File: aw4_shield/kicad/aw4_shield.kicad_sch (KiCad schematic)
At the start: 73 parts, among them J1 J1 +12V / PGND, J2 JP1 5V -> Nano (jumper), J3 J6 rezerva, J4 J2 SOL1-3 / TCU1-3, J5 J3 UP DOWN READY LOCKUP, J6 J5 Nextion +5V GND RX TX, K1 G5LE-1 12V SPDT, K2 G5LE-1 12V SPDT, K3 G5LE-1 12V SPDT, Q1 IRF4905, Q2 BC337, Q3 IRF9540N, Q4 IRF9540N, Q5 IRF9540N, U1 Buck 12V->5V 1A (modul), U2 Arduino Nano, U3 PC817, U4 PC817, U5 PC817, U6 PC817

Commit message: AW4 shield: connector references match docs
Co-Authored-By: Claude Sonnet 5.5 <noreply@anthropic.com>
Claude-Session: https://claude.ai/code/session_01QHDQqfFe1juWLgZ1EWa6E5
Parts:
- removed J2: JP1 5V -> Nano (jumper), Connector_PinHeader_2.54mm:PinHeader_1x02_P2.54mm_Vertical, symbol AW4:CONN2
- removed J3: J6 rezerva, Connector_PinHeader_2.54mm:PinHeader_1x07_P2.54mm_Vertical, symbol AW4:CONN7
- removed J4: J2 SOL1-3 / TCU1-3, TerminalBlock_Phoenix:TerminalBlock_Phoenix_MKDS-1,5-6-5.08_1x06_P5.08mm_Horizontal, symbol AW4:CONN6
- removed J5: J3 UP DOWN READY LOCKUP, TerminalBlock_Phoenix:TerminalBlock_Phoenix_MKDS-1,5-6-5.08_1x06_P5.08mm_Horizontal, symbol AW4:CONN6
- removed J6: J5 Nextion +5V GND RX TX, Connector_JST:JST_XH_B4B-XH-A_1x04_P2.50mm_Vertical, symbol AW4:CONN4
- added J2: J2 SOL1-3 / TCU1-3, TerminalBlock_Phoenix:TerminalBlock_Phoenix_MKDS-1,5-6-5.08_1x06_P5.08mm_Horizontal, symbol AW4:CONN6
- added J3: J3 UP DOWN READY LOCKUP, TerminalBlock_Phoenix:TerminalBlock_Phoenix_MKDS-1,5-6-5.08_1x06_P5.08mm_Horizontal, symbol AW4:CONN6
- added J5: J5 Nextion +5V GND RX TX, Connector_JST:JST_XH_B4B-XH-A_1x04_P2.50mm_Vertical, symbol AW4:CONN4
- added J6: J6 rezerva, Connector_PinHeader_2.54mm:PinHeader_1x07_P2.54mm_Vertical, symbol AW4:CONN7
- added JP1: JP1 5V -> Nano (jumper), Connector_PinHeader_2.54mm:PinHeader_1x02_P2.54mm_Vertical, symbol AW4:CONN2
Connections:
- net +5V: now also J3.1, JP1.1
- net +5V_DISP: now also J5.1
- net A0: now also J6.3
- net A1: now also J6.4
- net A2: now also J6.5
- net A3: now also J6.6
- net D12: now also J6.1
- net D13: now also J6.2
- net DISP_RX: now also J5.3
- net DISP_TX: now also J5.4
- net DOWN_IN: now also J3.4
- net GND: now also J3.2, J5.2, J6.7
- net LOCKUP_IN: now also J3.6
- net NANO_5V: now also JP1.2
- net READY_IN: now also J3.5
- net SOL1_OUT: now also J2.1
- net SOL2_OUT: now also J2.2
- net SOL3_OUT: now also J2.3
- net TCU1: now also J2.4
- net TCU2: now also J2.5
- net TCU3: now also J2.6
- net UP_IN: now also J3.3

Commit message: AW4 shield: routed PCB (KiCad 10 verified), Gerbers, TSR regulator, docs refresh
- KiCad project: schematic + 2-layer PCB 145x100 mm, autorouted, PGND/GND pours
- ERC 0/0, DRC 0 violations, 0 unconnected, 0 schematic parity issues (KiCad 10.0.6)
- Gerbers + drill in fab/, KiCad schematic PDF, PCB PDF and 3D renders in docs/
- 5 V from Traco TSR 1-2450 instead of a buck module on a header
- BC337 on TO-92_Inline_Wide (pad clearance), relay pinout checked against KiCad G5LE-1
- firmware: relay output D8 is active LOW
- generator scripts in tools/

Co-Authored-By: Claude Opus 5.5 <noreply@anthropic.com>
Claude-Session: https://claude.ai/code/session_01QHDQqfFe1juWLgZ1EWa6E5
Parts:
- removed C3: 47uF 10V, Capacitor_THT:CP_Radial_D6.3mm_P2.50mm, symbol AW4:CP
- removed C4, C9: 100nF, Capacitor_SMD:C_0805_2012Metric, symbol AW4:C
- removed C8: 100uF 10V, Capacitor_THT:CP_Radial_D6.3mm_P2.50mm, symbol AW4:CP
- removed U1: Buck 12V->5V 1A (modul), Connector_PinHeader_2.54mm:PinHeader_1x04_P2.54mm_Vertical, symbol AW4:BUCK_MODULE
- added C10, C8: 100nF, Capacitor_SMD:C_0805_2012Metric, symbol AW4:C
- added C3: 10uF 25V, Capacitor_SMD:C_1206_3216Metric, symbol AW4:C
- added C4: 47uF 10V, Capacitor_THT:CP_Radial_D6.3mm_P2.50mm, symbol AW4:CP
- added C9: 100uF 10V, Capacitor_THT:CP_Radial_D6.3mm_P2.50mm, symbol AW4:CP
- added U1: TSR 1-2450 (12V->5V 1A), Converter_DCDC:Converter_DCDC_TRACO_TSR-1_THT, symbol AW4:REG_5V
- Q2: footprint Package_TO_SOT_THT:TO-92_Inline -> Package_TO_SOT_THT:TO-92_Inline_Wide
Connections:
- net +12V_SW: now also C3.1, U1.1 (VIN)
- net +5V: now also C4.1
- net +5V_BUCK: now also U1.3 (VOUT)
- net +5V_DISP: now also C10.1, C9.1
- net DOWN_D: now also C6.1; no longer C5.1
- net GND: now also C10.2, C3.2, C4.2, C8.2, C9.2, U1.2 (GND)
- net LOCKUP_D: now also C8.1; no longer C7.1
- net READY_D: now also C7.1; no longer C6.1
- net UP_D: now also C5.1
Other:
- note added: "NAPÁJENÍ: +12V → F1 → Q0 (ochrana proti přepólování) → +12V_SW; TSR 1-2450 → +5V; PGND ↔ GND jen přes R 0R (hvězda)"
- note removed: "NAPÁJENÍ: +12V → F1 → Q0 (ochrana proti přepólování) → +12V_SW; buck modul → +5V; PGND ↔ GND jen přes R (hvězda)"

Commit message: AW4 shield v0.3: all through-hole parts, 100x100 mm board, values on silkscreen, order list
- every SMD part replaced by a through-hole one (vertical resistors/diodes,
  P6KE27A, 1N4007, BZX55 zeners, disc/radial caps, TR5 fuse holder)
- re-placed and re-routed on 100x100 mm; ERC/DRC/parity clean in KiCad 10.0.6
- silkscreen prints what to fit (value) at each part; references on F.Fab
- bom_objednavka.xlsx: order list with board-count multiplier + assembly order
- interactive BOM (docs/aw4_shield_ibom.html) and assembly drawing PDF

Co-Authored-By: Claude Opus 5.5 <noreply@anthropic.com>
Claude-Session: https://claude.ai/code/session_01QHDQqfFe1juWLgZ1EWa6E5
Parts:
- removed C3: 10uF 25V, Capacitor_SMD:C_1206_3216Metric, symbol AW4:C
- added C3: 10uF 25V, Capacitor_THT:CP_Radial_D5.0mm_P2.00mm, symbol AW4:CP
- C10, C2, C5, C6, C7, C8: footprint Capacitor_SMD:C_0805_2012Metric -> Capacitor_THT:C_Disc_D3.0mm_W2.0mm_P2.50mm
- D1: value BZT52C12 -> BZX55C12; footprint Diode_SMD:D_SOD-123 -> Diode_THT:D_DO-35_SOD27_P2.54mm_Vertical_CathodeUp
- D11, D13, D15: value BZT52C15 -> BZX55C15; footprint Diode_SMD:D_SOD-123 -> Diode_THT:D_DO-35_SOD27_P2.54mm_Vertical_CathodeUp
- D12, D14, D16: value SS34 -> 1N4007; footprint Diode_SMD:D_SMA -> Diode_THT:D_DO-41_SOD81_P5.08mm_Vertical_CathodeUp
- D2: value SMBJ24A -> P6KE27A; footprint Diode_SMD:D_SMB -> Diode_THT:D_DO-15_P5.08mm_Vertical_CathodeUp
- D3, D4, D5, D6, D7, D8: value PESD5V0S1BL -> BZX55C5V6; footprint Diode_SMD:D_SOD-323 -> Diode_THT:D_DO-35_SOD27_P2.54mm_Vertical_CathodeUp
- D9: value 1N4148W -> 1N4148; footprint Diode_SMD:D_SOD-123 -> Diode_THT:D_DO-35_SOD27_P2.54mm_Vertical_CathodeUp
- F1: footprint Fuse:Fuseholder_Cylinder-5x20mm_Schurter_0031_8201_Horizontal_Open -> Fuse:Fuseholder_TR5_Littelfuse_No560_No460
- L1, L2: footprint Inductor_SMD:L_0805_2012Metric -> Resistor_THT:R_Axial_DIN0207_L6.3mm_D2.5mm_P2.54mm_Vertical
- R1, R10, R11, R12, R13, R14, R15, R16, R17, R18, R19, R2, R20, R21, R22, R23, R24, R25, R3, R4, R5, R6, R7, R8, R9: footprint Resistor_SMD:R_0805_2012Metric -> Resistor_THT:R_Axial_DIN0207_L6.3mm_D2.5mm_P2.54mm_Vertical
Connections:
- net +12V_SW: now also C3.1
- net GND: now also C3.2

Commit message: AW4 shield: R14 220R -> 2k2 (opto/base current limit), design review notes
With a high-CTR PC817 the relay driver could push ~50 mA through R14 (0.55 W
in a 0.25 W resistor). 2k2 limits base current to ~5 mA, still enough for
the 90 mA relay coils with BC337.

Co-Authored-By: Claude Opus 5.5 <noreply@anthropic.com>
Claude-Session: https://claude.ai/code/session_01QHDQqfFe1juWLgZ1EWa6E5
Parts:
- R14: value 220 -> 2k2

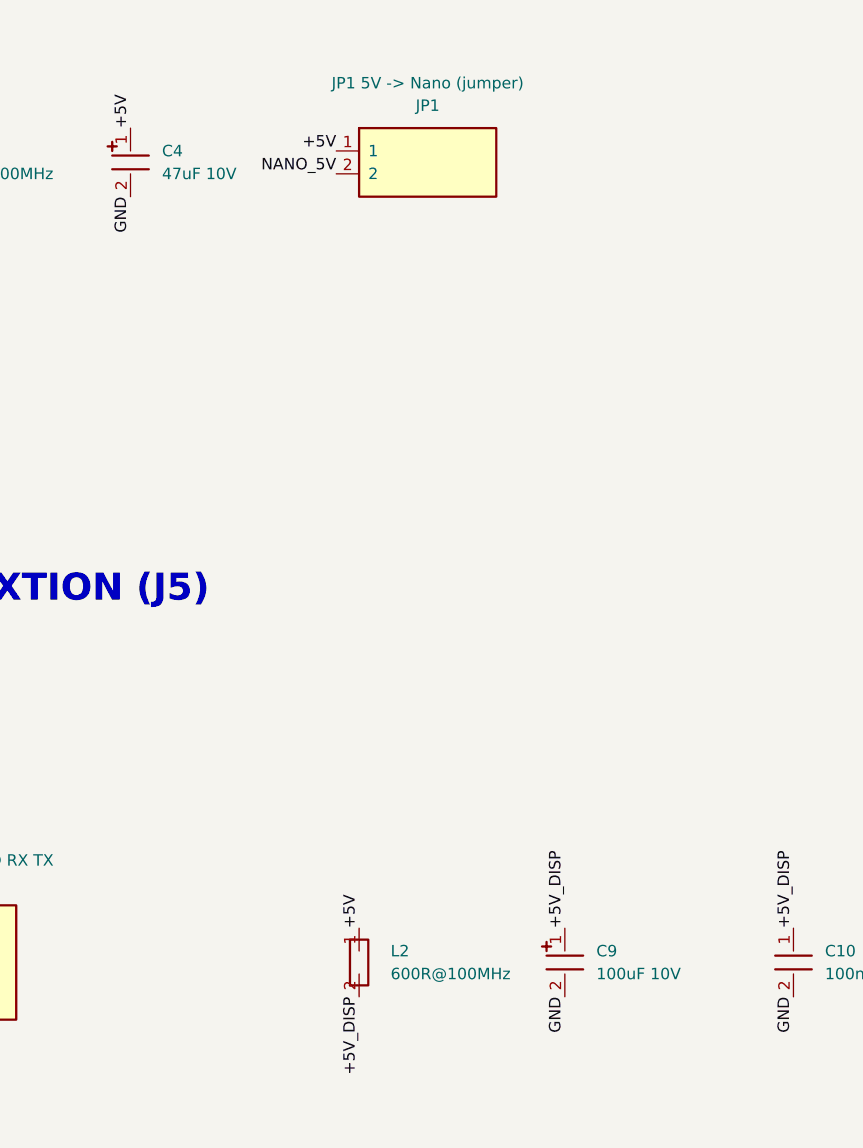
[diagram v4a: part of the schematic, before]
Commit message: AW4 shield: DigiKey BOM (CSV for BOM Manager + xlsx sheet), C4/C9 100uF 16V
- digikey_bom.csv with manufacturer part numbers for every part, matched by
  DigiKey BOM Manager; DigiKey sheet in bom_objednavka.xlsx scales with board count
- C4 47uF/10V -> 100uF/16V so both 6.3 mm caps are the same part and match
  the footprint; board regenerated, ERC/DRC/parity still clean

Co-Authored-By: Claude Opus 5.5 <noreply@anthropic.com>
Claude-Session: https://claude.ai/code/session_01QHDQqfFe1juWLgZ1EWa6E5
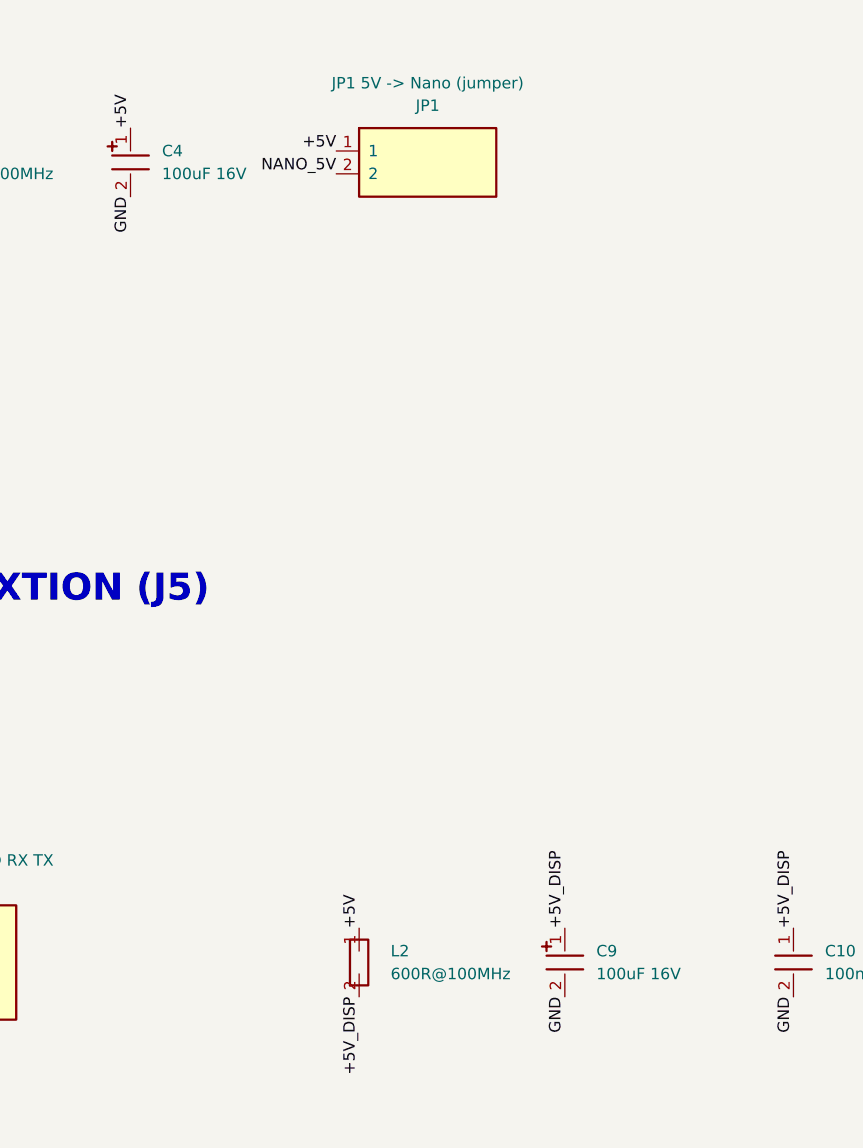
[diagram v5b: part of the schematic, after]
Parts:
- C4: value 47uF 10V -> 100uF 16V
- C9: value 100uF 10V -> 100uF 16V
